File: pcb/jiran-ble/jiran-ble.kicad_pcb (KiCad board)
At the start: 2 copper layers, 326.2 x 104.8 mm, 170 parts, among them J1 BATT, J2 USB-C Conn, J3 SWD, J4 BATT, J5 USB-C Conn, J6 SWD, P1 Breakoff, P2 Breakoff, P3 Breakoff, P4 Breakoff, Q1 AO3407, Q3 AO3407, SW1 SW_PUSH, SW10 SW_Push, SW11 SW_Push, SW12 SW_Push, SW13 SW_Push, SW14 SW_Push, SW15 SW_Push, SW16 SW_Push, SW17 SW_Push, SW18 SW_Push, SW19 SW_Push, SW2 SW_Push, SW20 SW_Push, SW21 SW_Push, SW22 SW_Push, SW23 SW_Push, SW24 SW_Push, SW25 SW_Push, SW26 SW_Push, SW27 SW_Push, SW28 SW_Push, SW29 SW_Push, SW3 SW_Push, SW30 SW_PUSH, SW31 SW_Push, SW32 SW_Push, SW33 SW_Push, SW34 SW_Push, SW35 SW_Push, SW36 SW_Push, SW37 SW_Push, SW38 SW_Push, SW39 SW_Push, SW4 SW_Push, SW40 SW_Push, SW41 SW_Push, SW42 SW_Push, SW43 SW_Push, SW44 SW_Push, SW45 SW_Push, SW46 SW_Push, SW47 SW_Push, SW48 SW_Push, SW49 SW_Push, SW5 SW_Push, SW50 SW_Push, SW51 SW_Push, SW52 SW_Push, SW53 SW_Push, SW54 SW_Push, SW55 SW_Push, SW56 SW_Push, SW57 SW_Push, SW58 SW_Push, SW6 SW_Push, SW7 SW_Push, SW8 SW_Push, SW9 SW_Push, U1 XC6220B331MR-G, U2 E73-2G4M08S1C, U3 TP4054, U4 XC6220B331MR-G, U5 E73-2G4M08S1C, U6 TP4054, X1 Crystal, X2 Crystal

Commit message: Delete tracks and zones
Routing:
- net /P0.29_l: track 269.1 -> 0.00 mm, vias 1 -> 0
- net /P0.29_r: track 257.0 -> 0.00 mm, vias 1 -> 0
- net GND: track 222.4 -> 0.00 mm, vias 1 -> 0
- net /P1.13_l: track 211.2 -> 0.00 mm, vias 3 -> 0
- net /P0.02_l: track 211.0 -> 0.00 mm, vias 3 -> 0
- net /P0.31_l: track 205.6 -> 0.00 mm, vias 1 -> 0
- net /P0.02_r: track 203.3 -> 0.00 mm, vias 1 -> 0
- net /P1.11_r: track 202.6 -> 0.00 mm, vias 1 -> 0
- net /P0.31_r: track 197.5 -> 0.00 mm, vias 1 -> 0
- net /P1.11_l: track 192.1 -> 0.00 mm, vias 1 -> 0
- net /P0.09_r: track 183.6 -> 0.00 mm, vias 1 -> 0
- net /P0.30_r: track 175.1 -> 0.00 mm, vias 1 -> 0
- net /P0.28_l: track 174.5 -> 0.00 mm, vias 5 -> 0
- net /P0.12_r: track 174.1 -> 0.00 mm
- net /P0.08_r: track 173.5 -> 0.00 mm, vias 3 -> 0
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- removed copper zone on B.Cu, net (none)
- removed copper zone on F.Cu, net (none)

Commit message: Version update
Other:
- net class Default removed

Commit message: Cache and backups update
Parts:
- removed G3, G4: LOGO, jiran-ble:logotype_rev
- removed P1, P2, P3, P4: Breakoff, jiran-ble:Panel_2x5
- removed Q3: AO3407, jiran-ble:Package_SMD_SOT-23
- removed R17: 1K, jiran-ble:Resistor_SMD_0805
- removed R18: RPROG, jiran-ble:Resistor_SMD_0805
- removed X1, X2: Crystal, jiran-ble:Crystal_SMD_CM9V
- added C1: 10uF, jiran-ble:C_0402, F.Cu at (219.7, 5.82)
- added C2: 10uF, jiran-ble:C_0402, F.Cu at (213.0, 12.4)
- added C3: 10uF, jiran-ble:C_0402, F.Cu at (219.7, 7.79)
- added C4: 10uF, jiran-ble:C_0402, F.Cu at (218.1, 10.4)
- added Q2: SI2301CDS-T1-GE3, jiran-ble:SOT-23, F.Cu at (216.1, 7.11)
- added R14: 1k, jiran-ble:R_0402, F.Cu at (215.2, 10.4)
- added R6: 2M, jiran-ble:R_0603, F.Cu at (209.5, 11.0)
- added SW59: SW_Push, jiran-ble:TS-1086E, F.Cu at (210.6, 7.48)
- D1, D30: footprint jiran-ble:Diode_SMD_SOD-123 -> jiran-ble:D_SOD-123
- D10, D11, D12, D13, D14, D15, D16, D17, D18, D19, D2, D20, D21, D22, D23, D24, D25, D26, D27, D28, D29, D3, D31, D32, D33, D34, D35, D36, D37, D38, D39, D4, D40, D41, D42, D43, D44, D45, D46, D47, D48, D49, D5, D50, D51, D52, D53, D54, D55, D56, D57, D58, D6, D7, D8, D9: value 1N4148 -> 1N5819; footprint jiran-ble:Diode_SMD_SOD-123 -> jiran-ble:D_SOD-123
- J1, J4: footprint jiran-ble:Connector_THT_1x2_2.54 -> jiran-ble:JST_ZH_1x2_P1.5
- J2, J5: value USB-C Conn -> USB-C Connector; footprint jiran-ble:USB-C_MidMount -> jiran-ble:USB-C-31-M-27
- LED1, LED2, LED3, LED4: footprint jiran-ble:LED_SMD_0805 -> jiran-ble:LED_0603
- Q1: value AO3407 -> SI2301CDS-T1-GE3; footprint jiran-ble:Package_SMD_SOT-23 -> jiran-ble:SOT-23
- R1, R10, R2: value 5.1K -> 5.1k; footprint jiran-ble:Resistor_SMD_0805 -> jiran-ble:R_0402
- R11: value 5.1K -> 750K; footprint jiran-ble:Resistor_SMD_0805 -> jiran-ble:R_0603
- R12, R5: value 820K -> 100K; footprint jiran-ble:Resistor_SMD_0805 -> jiran-ble:R_0402
- R13: value 1K -> 2M; footprint jiran-ble:Resistor_SMD_0805 -> jiran-ble:R_0603
- R15, R4: value 100K -> 1k; footprint jiran-ble:Resistor_SMD_0805 -> jiran-ble:R_0402
- R16: value 2M -> 10k; footprint jiran-ble:Resistor_SMD_0805 -> jiran-ble:R_0402
- R3: value 1K -> 750K; footprint jiran-ble:Resistor_SMD_0805 -> jiran-ble:R_0603
- R7: value 2M -> 1k; footprint jiran-ble:Resistor_SMD_0805 -> jiran-ble:R_0402
- R8: value 1K -> 10k; footprint jiran-ble:Resistor_SMD_0805 -> jiran-ble:R_0402
- R9: value RPROG -> 5.1k; footprint jiran-ble:Resistor_SMD_0805 -> jiran-ble:R_0402
- SW1: value SW_PUSH -> SW_DPDT_x2; footprint jiran-ble:Switch_SMD_Tact_3-6-3,5 -> jiran-ble:MSK-12C02
- SW30: value SW_PUSH -> SW_Push; footprint jiran-ble:Switch_SMD_Tact_3-6-3,5 -> jiran-ble:Switch_Mx_Hotswap_1u
- SW58: footprint jiran-ble:Switch_Mx_Hotswap_1u -> jiran-ble:TS-1086E
- U1, U4: value XC6220B331MR-G -> HOLYIOT-18010-NRF52840_simple; footprint jiran-ble:Package_SMD_SOT-23-5 -> jiran-ble:Holyiot-18010-nRF52840
- U2, U5: value E73-2G4M08S1C -> XC6220B331MR-G; footprint jiran-ble:E73-2G4M08S1C-52840 -> jiran-ble:SOT-23-5
- U3, U6: footprint jiran-ble:Package_SMD_SOT-23-5 -> jiran-ble:SOT-23-5
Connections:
- D1 pad 1: Net-(D1-Pad1) -> Net-(C1-Pad1)
- D10 pad 1: /P0.28_l -> /P0.21_l
- D11 pad 1: /P0.28_l -> /P0.21_l
- D12 pad 1: /P0.28_l -> /P0.21_l
- D13 pad 1: /P0.28_l -> /P0.21_l
- D14 pad 1: /P1.13_l -> /P0.19_l
- D15 pad 1: /P1.13_l -> /P0.19_l
- D16 pad 1: /P1.13_l -> /P0.19_l
- D17 pad 1: /P1.13_l -> /P0.19_l
- D18 pad 1: /P1.13_l -> /P0.19_l
- D19 pad 1: /P1.13_l -> /P0.19_l
- D2 pad 1: /P1.11_l -> /P0.23_l
- D20 pad 1: /P0.02_l -> /P1.03_l
- D21 pad 1: /P0.02_l -> /P1.03_l
- D22 pad 1: /P0.02_l -> /P1.03_l
- D23 pad 1: /P0.02_l -> /P1.03_l
- D24 pad 1: /P0.02_l -> /P1.03_l
- D25 pad 1: /P0.02_l -> /P1.03_l
- D26 pad 1: /P0.29_l -> /P1.01_l
- D27 pad 1: /P0.29_l -> /P1.01_l
- D28 pad 1: /P0.29_l -> /P1.01_l
- D29 pad 1: /P0.29_l -> /P1.01_l
- D3 pad 1: /P1.11_l -> /P0.23_l
- D30 pad 1: Net-(D30-Pad1) -> /P0.23_r
- D30 pad 2: VBUS_r -> Net-(D30-Pad2)
- D31 pad 1: /P1.11_r -> /P0.23_r
- D32 pad 1: /P1.11_r -> /P0.23_r
- D33 pad 1: /P1.11_r -> /P0.23_r
- D34 pad 1: /P1.11_r -> /P0.23_r
- D35 pad 1: /P1.11_r -> /P0.23_r
- D36 pad 1: /P1.11_r -> /P0.21_r
- D37 pad 1: /P0.28_r -> /P0.21_r
- D38 pad 1: /P0.28_r -> /P0.21_r
- D39 pad 1: /P0.28_r -> /P0.21_r
- D4 pad 1: /P1.11_l -> /P0.23_l
- D40 pad 1: /P0.28_r -> /P0.21_r
- D41 pad 1: /P0.28_r -> /P0.21_r
- D42 pad 1: /P0.28_r -> /P0.19_r
- D43 pad 1: /P1.13_r -> /P0.19_r
- D44 pad 1: /P1.13_r -> /P0.19_r
- D45 pad 1: /P1.13_r -> /P0.19_r
- D46 pad 1: /P1.13_r -> /P0.19_r
- D47 pad 1: /P1.13_r -> /P0.19_r
- D48 pad 1: /P1.13_r -> /P1.03_r
- D49 pad 1: /P0.02_r -> /P1.03_r
- D5 pad 1: /P1.11_l -> /P0.23_l
- D50 pad 1: /P0.02_r -> /P1.03_r
- D51 pad 1: /P0.02_r -> /P1.03_r
- D52 pad 1: /P0.02_r -> /P1.03_r
- D53 pad 1: /P0.02_r -> /P1.03_r
- D54 pad 1: /P0.02_r -> /P1.01_r
- D55 pad 1: /P0.29_r -> /P1.01_r
- D56 pad 1: /P0.29_r -> /P1.01_r
- D57 pad 1: /P0.29_r -> /P1.01_r
- D58 pad 1: /P0.29_r -> Net-(C3-Pad1)
- D58 pad 2: Net-(D58-Pad2) -> VBUS_r
- D6 pad 1: /P1.11_l -> /P0.23_l
- D7 pad 1: /P1.11_l -> /P0.23_l
- D8 pad 1: /P0.28_l -> /P0.21_l
- D9 pad 1: /P0.28_l -> /P0.21_l
- J2 pad A6: DATA+_l -> D+_l
- J2 pad A7: DATA-_l -> D-_l
- J2 pad B6: DATA+_l -> D+_l
- J2 pad B7: DATA-_l -> D-_l
- J2 pad S1: GND -> unconnected-(J2-PadS1)
- J5 pad A6: DATA+_r -> D+_r
- J5 pad A7: DATA-_r -> D-_r
- J5 pad B6: DATA+_r -> D+_r
- J5 pad B7: DATA-_r -> D-_r
- J5 pad S1: GND -> unconnected-(J5-PadS1)
- Q1 pad 2: Net-(D1-Pad1) -> Net-(C1-Pad1)
- Q1 pad 3: VBAT_l -> Net-(Q1-Pad3)
- R10 pad 1: Net-(J5-PadA5) -> GND
- R10 pad 2: GND -> Net-(J5-PadB5)
- R11 pad 1: Net-(J5-PadB5) -> VBAT_r
- R11 pad 2: GND -> BATTERY_PIN_r
- R12 pad 1: VBAT_r -> VBUS_r
- R12 pad 2: BATTERY_PIN_r -> GND
- R13 pad 1: Net-(LED3-Pad1) -> BATTERY_PIN_r
- R15 pad 1: VBUS_r -> Net-(LED4-Pad1)
- R15 pad 2: GND -> Net-(R15-Pad2)
- R16 pad 1: BATTERY_PIN_r -> Net-(R16-Pad1)
- R2 pad 1: Net-(J2-PadB5) -> GND
- R2 pad 2: GND -> Net-(J2-PadB5)
- R3 pad 1: Net-(LED1-Pad1) -> VBAT_l
- R3 pad 2: GND -> BATTERY_PIN_l
- R4 pad 1: VBUS_l -> GND
- R4 pad 2: GND -> Net-(LED1-Pad1)
- R5 pad 1: VBAT_l -> VBUS_l
- R5 pad 2: BATTERY_PIN_l -> GND
- R7 pad 1: BATTERY_PIN_l -> Net-(LED2-Pad1)
- R7 pad 2: GND -> Net-(R7-Pad2)
- R8 pad 1: Net-(LED2-Pad1) -> Net-(R8-Pad1)
- R8 pad 2: Net-(R8-Pad2) -> GND
- R9 pad 1: Net-(R9-Pad1) -> Net-(J5-PadA5)
- SW1 pad 1: RESET_l -> unconnected-(SW1-Pad1)
- SW1 pad 2: GND -> VBAT_l
- SW10 pad 2: /P0.06_l -> /P0.28_l
- SW11 pad 2: /P0.08_l -> /P0.29_l
- SW12 pad 2: /P0.09_l -> /P0.30_l
- SW13 pad 2: /P0.12_l -> /P0.31_l
- SW14 pad 2: /P0.31_l -> /P0.03_l
- SW15 pad 2: /P0.30_l -> /P0.02_l
- SW16 pad 2: /P0.06_l -> /P0.28_l
- SW17 pad 2: /P0.08_l -> /P0.29_l
- SW18 pad 2: /P0.09_l -> /P0.30_l
- SW19 pad 2: /P0.12_l -> /P0.31_l
- SW2 pad 2: /P0.31_l -> /P0.03_l
- SW20 pad 2: /P0.31_l -> /P0.03_l
- SW21 pad 2: /P0.30_l -> /P0.02_l
- SW22 pad 2: /P0.06_l -> /P0.28_l
- SW23 pad 2: /P0.08_l -> /P0.29_l
- SW24 pad 2: /P0.09_l -> /P0.30_l
- SW25 pad 2: /P0.12_l -> /P0.31_l
- SW26 pad 2: /P0.31_l -> /P0.03_l
- SW27 pad 2: /P0.08_l -> /P0.29_l
- SW28 pad 2: /P0.09_l -> /P0.30_l
- SW29 pad 2: /P0.12_l -> /P0.31_l
- SW3 pad 2: /P0.30_l -> /P0.02_l
- SW30 pad 1: RESET_r -> Net-(D30-Pad2)
- SW30 pad 2: GND -> /P0.03_r
- SW31 pad 2: /P0.31_r -> /P0.02_r
- SW32 pad 2: /P0.30_r -> /P0.28_r
- SW33 pad 2: /P0.06_r -> /P0.29_r
- SW34 pad 2: /P0.08_r -> /P0.30_r
- SW35 pad 2: /P0.09_r -> /P0.31_r
- SW36 pad 2: /P0.12_r -> /P0.03_r
- SW37 pad 2: /P0.31_r -> /P0.02_r
- SW38 pad 2: /P0.30_r -> /P0.28_r
- SW39 pad 2: /P0.06_r -> /P0.29_r
- SW4 pad 2: /P0.06_l -> /P0.28_l
- SW40 pad 2: /P0.08_r -> /P0.30_r
- SW41 pad 2: /P0.09_r -> /P0.31_r
- SW42 pad 2: /P0.12_r -> /P0.03_r
- SW43 pad 2: /P0.31_r -> /P0.02_r
- SW44 pad 2: /P0.30_r -> /P0.28_r
- SW45 pad 2: /P0.06_r -> /P0.29_r
- SW46 pad 2: /P0.08_r -> /P0.30_r
- SW47 pad 2: /P0.09_r -> /P0.31_r
- SW48 pad 2: /P0.12_r -> /P0.03_r
- SW49 pad 2: /P0.31_r -> /P0.02_r
- SW5 pad 2: /P0.08_l -> /P0.29_l
- SW50 pad 2: /P0.30_r -> /P0.28_r
- SW51 pad 2: /P0.06_r -> /P0.29_r
- SW52 pad 2: /P0.08_r -> /P0.30_r
- SW53 pad 2: /P0.09_r -> /P0.31_r
- SW54 pad 2: /P0.12_r -> /P0.03_r
- SW55 pad 2: /P0.31_r -> /P0.29_r
- SW56 pad 2: /P0.08_r -> /P0.30_r
- SW57 pad 2: /P0.09_r -> /P0.31_r
- SW58 pad 1: Net-(D58-Pad2) -> RESET_l
- SW58 pad 2: /P0.12_r -> GND
- SW6 pad 2: /P0.09_l -> /P0.30_l
- SW7 pad 2: /P0.12_l -> /P0.31_l
- SW8 pad 2: /P0.31_l -> /P0.03_l
- SW9 pad 2: /P0.30_l -> /P0.02_l
- U1 pad 1: Net-(D1-Pad1) -> GND
- U1 pad 2: GND -> unconnected-(U1-Pad2)
- U1 pad 3: Net-(D1-Pad1) -> BLUE_LED_l
- U1 pad 4: (no net) -> unconnected-(U1-Pad4)
- U1 pad 5: nRF_VDD_l -> unconnected-(U1-Pad5)
- U2 pad 1: /P1.11_l -> Net-(C1-Pad1)
- U2 pad 2: BLUE_LED_l -> GND
- U2 pad 3: (no net) -> Net-(C1-Pad1)
- U2 pad 4: /P0.28_l -> unconnected-(U2-Pad4)
- U2 pad 5: GND -> nRF_VDD_l
- U3 pad 1: Net-(R8-Pad2) -> Net-(R7-Pad2)
- U3 pad 5: Net-(R9-Pad1) -> Net-(R8-Pad1)
- U4 pad 1: Net-(D30-Pad1) -> GND
- U4 pad 2: GND -> unconnected-(U4-Pad2)
- U4 pad 3: Net-(D30-Pad1) -> BLUE_LED_r
- U4 pad 4: (no net) -> unconnected-(U4-Pad4)
- U4 pad 5: nRF_VDD_r -> unconnected-(U4-Pad5)
- U5 pad 1: /P1.11_r -> Net-(C3-Pad1)
- U5 pad 2: BLUE_LED_r -> GND
- U5 pad 3: (no net) -> Net-(C3-Pad1)
- U5 pad 4: /P0.28_r -> unconnected-(U5-Pad4)
- U5 pad 5: GND -> nRF_VDD_r
- U6 pad 1: Net-(R17-Pad2) -> Net-(R15-Pad2)
- U6 pad 5: Net-(R18-Pad1) -> Net-(R16-Pad1)

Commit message: Backups update
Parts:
- added SW60: SW_DPDT, jiran-ble:MSK-12C02, F.Cu at (57.1, -157.1)
- D1, D30, Q1, U3, U6: moved to F.Cu
- G1: value logo-jiran-hotswap -> Logo-Jiran-BLE; moved to F.Cu
- G2: value logo-jiran-hotswap -> Logo-Jiran-BLE
- J2: value USB-C Connector -> USB-C-Receptacle; moved to B.Cu
- J5: value USB-C Connector -> USB-C-Receptacle
- SW1: value SW_DPDT_x2 -> SW_Push; footprint jiran-ble:MSK-12C02 -> jiran-ble:TS-1086E
- SW30: value SW_Push -> SW_DPDT; footprint jiran-ble:Switch_Mx_Hotswap_1u -> jiran-ble:MSK-12C02
- SW58: footprint jiran-ble:TS-1086E -> jiran-ble:Switch_Mx_Hotswap_1u
- U1: value HOLYIOT-18010-NRF52840_simple -> HOLYIOT-18010-NRF52840_Simple
- U2, U5: value XC6220B331MR-G -> AP2112K-3.3
- U4: value HOLYIOT-18010-NRF52840_simple -> HOLYIOT-18010-NRF52840_Simple; moved to F.Cu
- moved U4 285.5 mm to (40.1, -170.6), turned to 0 degrees
- moved J6 283.1 mm to (45.4, -154.3), turned to 0 degrees
- moved G2 278.6 mm to (23.2, -136.9)
- moved J4 270.4 mm to (64.6, -148.5), turned to 0 degrees
- moved SW30 267.9 mm to (57.1, -150.7), turned to 0 degrees
- moved R15 263.3 mm to (52.3, -143.4), turned to 0 degrees
- moved SW1 262.7 mm to (33.2, -145.1), turned to 0 degrees
- moved HM1 260.9 mm to (220.3, -132.7)
- moved LED4 260.8 mm to (61.8, -143.7), turned to 0 degrees
- moved J5 260.8 mm to (36.6, -153.9)
- moved HM4 259.8 mm to (205.3, -112.5)
- moved J1 255.7 mm to (64.6, -156.2), turned to 0 degrees
- moved J3 255.5 mm to (50.1, -154.3), turned to 0 degrees
- moved R16 255.0 mm to (68.8, -159.4), turned to 0 degrees
- moved LED2 253.8 mm to (32.2, -149.6), turned to 0 degrees
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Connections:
- D30 pad 1: /P0.23_r -> Net-(C3-Pad1)
- D30 pad 2: Net-(D30-Pad2) -> VBUS_r
- D36 pad 1: /P0.21_r -> /P0.23_r
- D42 pad 1: /P0.19_r -> /P0.21_r
- D48 pad 1: /P1.03_r -> /P0.19_r
- D54 pad 1: /P1.01_r -> /P1.03_r
- D58 pad 1: Net-(C3-Pad1) -> /P1.01_r
- D58 pad 2: VBUS_r -> Net-(D58-Pad2)
- SW1 pad 1: unconnected-(SW1-Pad1) -> RESET_l
- SW1 pad 2: VBAT_l -> GND
- SW1 pad 3: Net-(Q1-Pad3) -> (no net)
- SW1 pad 4: unconnected-(SW1-Pad4) -> (no net)
- SW30 pad 1: Net-(D30-Pad2) -> unconnected-(SW30-Pad1)
- SW30 pad 2: /P0.03_r -> VBAT_l
- SW31 pad 2: /P0.02_r -> /P0.03_r
- SW32 pad 2: /P0.28_r -> /P0.02_r
- SW33 pad 2: /P0.29_r -> /P0.28_r
- SW34 pad 2: /P0.30_r -> /P0.29_r
- SW35 pad 2: /P0.31_r -> /P0.30_r
- SW36 pad 2: /P0.03_r -> /P0.31_r
- SW37 pad 2: /P0.02_r -> /P0.03_r
- SW38 pad 2: /P0.28_r -> /P0.02_r
- SW39 pad 2: /P0.29_r -> /P0.28_r
- SW40 pad 2: /P0.30_r -> /P0.29_r
- SW41 pad 2: /P0.31_r -> /P0.30_r
- SW42 pad 2: /P0.03_r -> /P0.31_r
- SW43 pad 2: /P0.02_r -> /P0.03_r
- SW44 pad 2: /P0.28_r -> /P0.02_r
- SW45 pad 2: /P0.29_r -> /P0.28_r
- SW46 pad 2: /P0.30_r -> /P0.29_r
- SW47 pad 2: /P0.31_r -> /P0.30_r
- SW48 pad 2: /P0.03_r -> /P0.31_r
- SW49 pad 2: /P0.02_r -> /P0.03_r
- SW50 pad 2: /P0.28_r -> /P0.02_r
- SW51 pad 2: /P0.29_r -> /P0.28_r
- SW52 pad 2: /P0.30_r -> /P0.29_r
- SW53 pad 2: /P0.31_r -> /P0.30_r
- SW54 pad 2: /P0.03_r -> /P0.31_r
- SW55 pad 2: /P0.29_r -> /P0.03_r
- SW56 pad 2: /P0.30_r -> /P0.29_r
- SW57 pad 2: /P0.31_r -> /P0.30_r
- SW58 pad 1: RESET_l -> Net-(D58-Pad2)
- SW58 pad 2: GND -> /P0.31_r
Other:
- board size 326.2 x 104.8 mm -> 152.4 x 104.6 mm

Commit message: Update footprints
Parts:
- D1, D30: value 1N5819 -> B5819W
- J2, J5: footprint jiran-ble:USB-C-31-M-27 -> jiran-ble:USB-C-31-M-12
- SW1, SW30: moved to B.Cu
- moved J3 288.5 mm to (183.0, 101.7)
- moved SW30 284.5 mm to (167.6, 111.4), turned to 90 degrees
- moved SW1 280.6 mm to (167.9, 101.1), turned to 90 degrees
- moved J1 279.4 mm to (155.6, 107.9)
- moved LED2 273.3 mm to (153.9, 95.1), turned to 90 degrees
- moved LED1 257.3 mm to (166.8, 93.1), turned to 90 degrees
- moved R7 255.9 mm to (153.3, 84.1), turned to -90 degrees
- moved R8 249.6 mm to (160.9, 84.1), turned to 90 degrees
- moved R1 247.5 mm to (153.3, 77.2), turned to -90 degrees
- moved R2 246.0 mm to (155.4, 76.8), turned to 180 degrees
- moved R4 245.5 mm to (158.2, 76.8)
- moved R5 243.5 mm to (153.3, 79.5), turned to -90 degrees
- moved R6 231.9 mm to (163.6, 86.1), turned to 180 degrees
- moved C1 174.3 mm to (160.9, 81.8), turned to -90 degrees
- moved Q1 172.8 mm to (164.0, 79.0), turned to 180 degrees
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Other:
- outline, holes or cut-outs redrawn

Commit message: Backups update
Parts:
- J2, SW1, SW30: moved to F.Cu
- moved HM1 265.4 mm to (131.2, 117.3)
- moved HM4 264.7 mm to (55.0, 105.4)
- moved HM5 258.7 mm to (35.9, 87.5)
- moved HM3 227.0 mm to (55.0, 67.3)
- moved HM2 177.5 mm to (131.2, 60.2)
- moved LED2 26.3 mm to (152.1, 68.8)
- moved LED1 24.3 mm to (167.4, 68.8)
- moved J3 17.6 mm to (166.8, 108.6), turned to 180 degrees
- moved J1 14.7 mm to (166.8, 117.6), turned to 180 degrees
- moved SW30 13.1 mm to (167.1, 98.3), turned to -90 degrees
- moved SW1 10.7 mm to (167.5, 90.4), turned to -90 degrees
- moved R8 4.22 mm to (159.4, 80.1)
- moved R7 3.94 mm to (153.3, 80.1), turned to 90 degrees
- moved Q1 2.25 mm to (162.4, 77.3), turned to 0 degrees
- moved R6 2.25 mm to (162.1, 84.5)
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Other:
- outline, holes or cut-outs redrawn

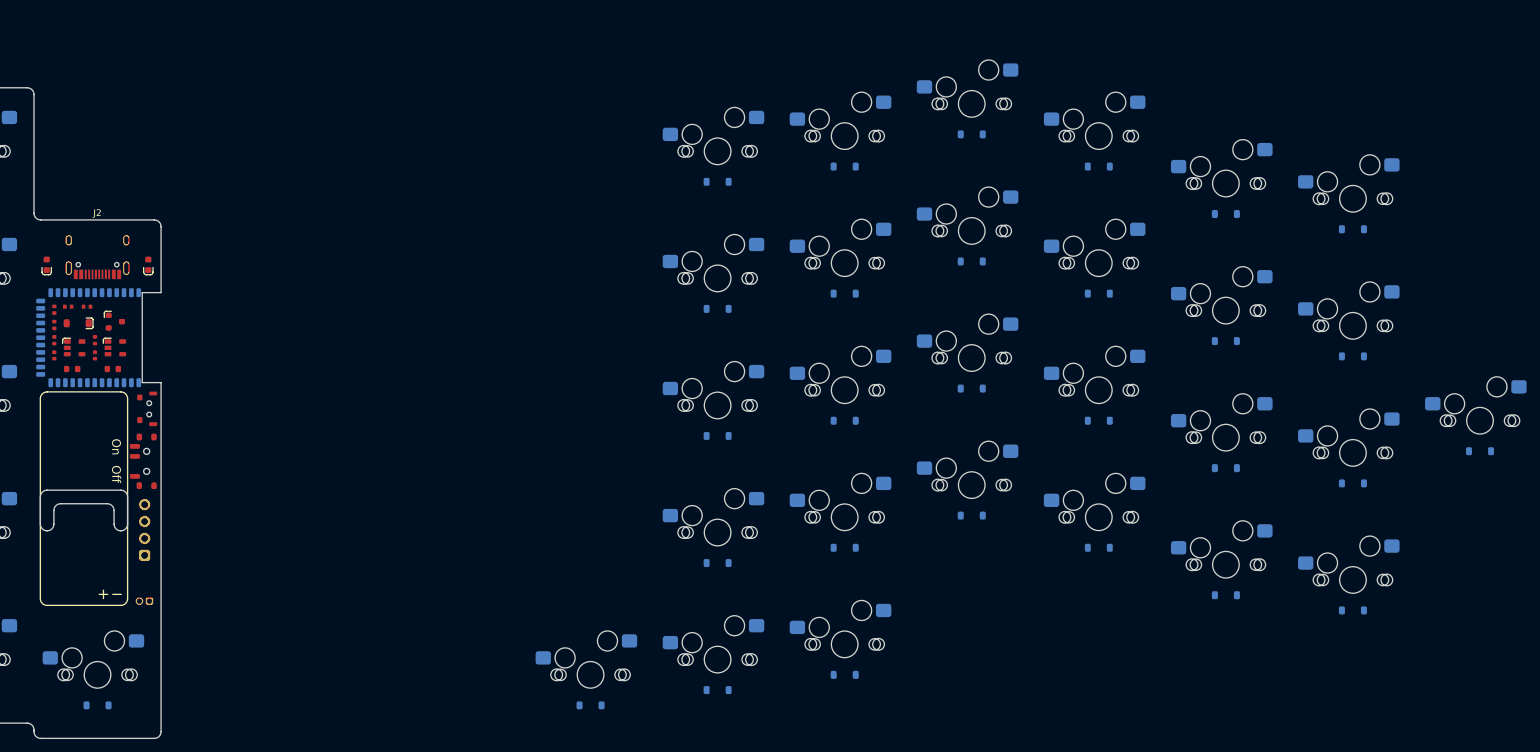
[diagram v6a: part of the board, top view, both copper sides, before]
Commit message: Draw edge.cuts
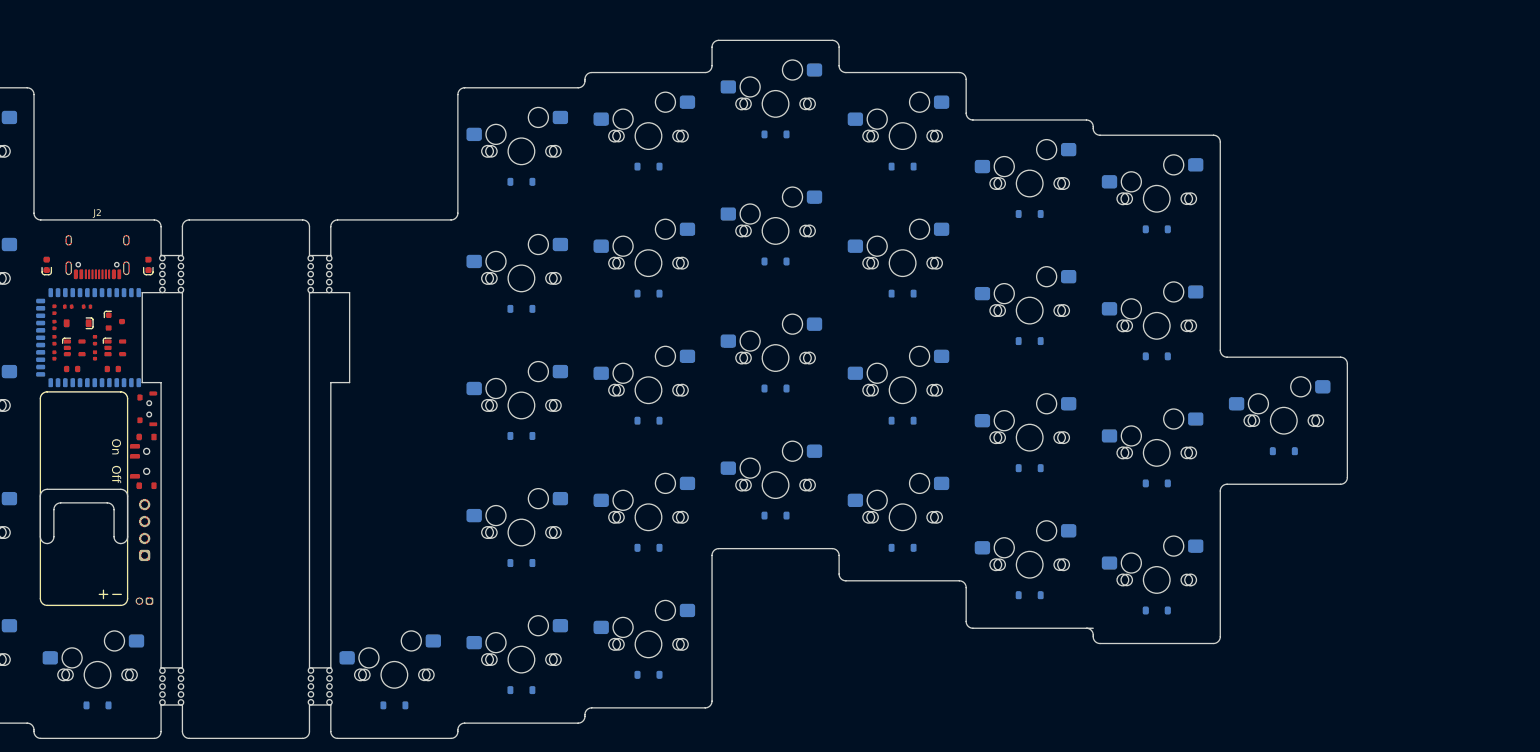
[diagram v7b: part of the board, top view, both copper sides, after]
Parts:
- added P1: Breakoff, jiran-ble:Panel_2x5, F.Cu at (170.9, 70.2)
- added P2: Breakoff, jiran-ble:Panel_2x5, F.Cu at (170.9, 132.1)
- added P3: Breakoff, jiran-ble:Panel_2x5, F.Cu at (193.1, 70.2)
- added P4: Breakoff, jiran-ble:Panel_2x5, F.Cu at (193.1, 132.0)
- moved D31 29.4 mm to (318.6, 63.5)
- moved D32 29.4 mm to (299.5, 61.2)
- moved D33 29.4 mm to (280.5, 54.1)
- moved D34 29.4 mm to (261.4, 49.3)
- moved D37 29.4 mm to (318.6, 82.5)
- moved D38 29.4 mm to (299.5, 80.3)
- moved D39 29.4 mm to (280.5, 73.2)
- moved D40 29.4 mm to (261.4, 68.3)
- moved D43 29.4 mm to (318.6, 101.6)
- moved D44 29.4 mm to (299.5, 99.3)
- moved D45 29.4 mm to (280.5, 92.2)
- moved D46 29.4 mm to (261.4, 87.4)
- moved D49 29.4 mm to (318.6, 120.6)
- moved D50 29.4 mm to (299.5, 118.4)
- moved D51 29.4 mm to (280.5, 111.3)
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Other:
- board size 152.4 x 104.6 mm -> 330.3 x 104.6 mm

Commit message: Place components on the right half, backups update
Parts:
- U4: moved to B.Cu
- moved J6 303.6 mm to (197.3, 108.6)
- moved U4 299.1 mm to (203.7, 79.7), turned to -90 degrees
- moved J4 297.4 mm to (197.2, 117.6), turned to 180 degrees
- moved SW60 291.2 mm to (196.9, 98.3), turned to 90 degrees
- moved SW59 286.0 mm to (196.8, 90.4), turned to 90 degrees
- moved R12 280.1 mm to (210.7, 77.9), turned to -90 degrees
- moved J5 276.8 mm to (204.3, 66.3)
- moved R15 275.8 mm to (210.7, 82.4), turned to 90 degrees
- moved R16 275.5 mm to (204.6, 80.3), turned to 90 degrees
- moved R14 264.8 mm to (205.8, 75.1)
- moved R10 264.6 mm to (208.6, 75.1)
- moved R9 264.4 mm to (210.7, 75.6), turned to -90 degrees
- moved LED4 260.1 mm to (211.8, 68.8), turned to 90 degrees
- moved HM6 256.7 mm to (232.8, 117.3)
- moved HM9 249.2 mm to (309.0, 105.4)
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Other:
- outline, holes or cut-outs redrawn
